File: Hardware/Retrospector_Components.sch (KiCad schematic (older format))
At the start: 147 parts, among them J1 Conn_01x08_Male, J2 Conn_01x08_Male, J3 Conn_01x08_Male, J4 Conn_01x08_Male, J5 SWD_Header, J6 USB_B_Micro, J7 Eurorack_10_pin_power, J8 I2C_TestPoint, U1 MCP6004, U10 LD1117-3.3-4Tab, U2 TL074, U3 MCP6004, U4 IS42S16800F-7TLI, U5 STM32H743ZITx, U6 TL072, U7 AS3364, U8 PCM5100APW, U9 LM2675M-5, Y1 8MHz 20pF

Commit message: Updates to control and panel PCBs
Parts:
- C43: footprint Capacitors_SMD:CP_Elec_5x5.7 -> Capacitors_SMD:CP_Elec_5x5.8; Part_Number C178597 -> (none)
- C61: footprint Capacitors_SMD:CP_Elec_4x5.8 -> Capacitors_SMD:CP_Elec_5x5.8; Part_Number C178597 -> (none)
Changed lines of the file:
@@
 F 0 "C61" H 4250 11700 50  0000 C CNN
 F 1 "47uF" H 4250 11600 50  0000 C CNN
-F 2 "Capacitors_SMD:CP_Elec_4x5.8" H 4438 11550 50  0001 C CNN
-F 3 "https://datasheet.lcsc.com/szlcsc/1809131544_PANASONIC-EEEFT1V220AR_C178597.pdf" H 4400 11700 50  0001 C CNN
-F 4 "C178597" H 4400 11700 50  0001 C CNN "Part_Number"
+F 2 "Capacitors_SMD:CP_Elec_5x5.8" H 4438 11550 50  0001 C CNN
+F 3 "" H 4400 11700 50  0001 C CNN
+F 4 "" H 4400 11700 50  0001 C CNN "Part_Number"
 F 5 "90" H 4400 11700 50  0001 C CNN "Rotation"
 	1    4400 11700
@@
 F 0 "C43" V 1695 9900 50  0000 C CNN
 F 1 "47uF" V 1786 9900 50  0000 C CNN
-F 2 "Capacitors_SMD:CP_Elec_5x5.7" H 1988 9750 50  0001 C CNN
-F 3 "https://datasheet.lcsc.com/szlcsc/1809131544_PANASONIC-EEEFT1V220AR_C178597.pdf" H 1950 9900 50  0001 C CNN
-F 4 "C178597" H 1950 9900 50  0001 C CNN "Part_Number"
+F 2 "Capacitors_SMD:CP_Elec_5x5.8" H 1988 9750 50  0001 C CNN
+F 3 "" H 1950 9900 50  0001 C CNN
+F 4 "" H 1950 9900 50  0001 C CNN "Part_Number"
 F 5 "360" H 1950 9900 50  0001 C CNN "Rotation"
 	1    1950 9900

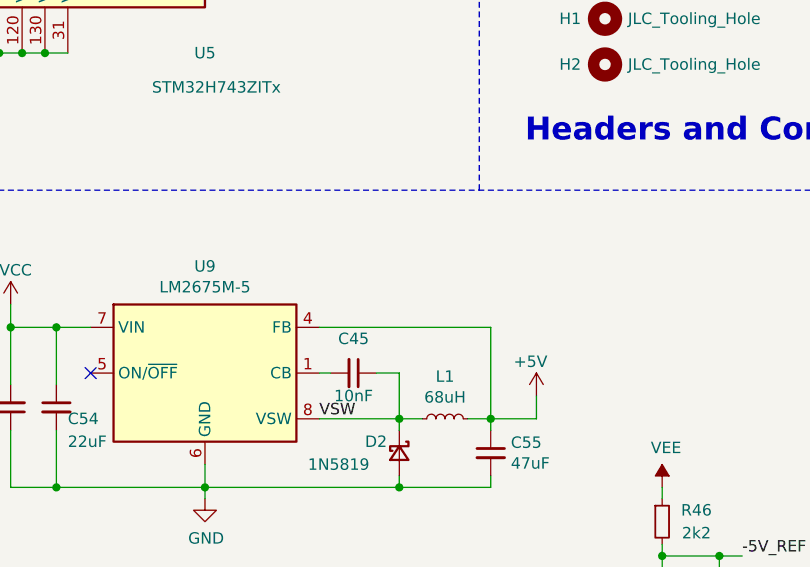
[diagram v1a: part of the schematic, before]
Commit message: Final updates to v2 PCBs for production; USB DFU Mode working
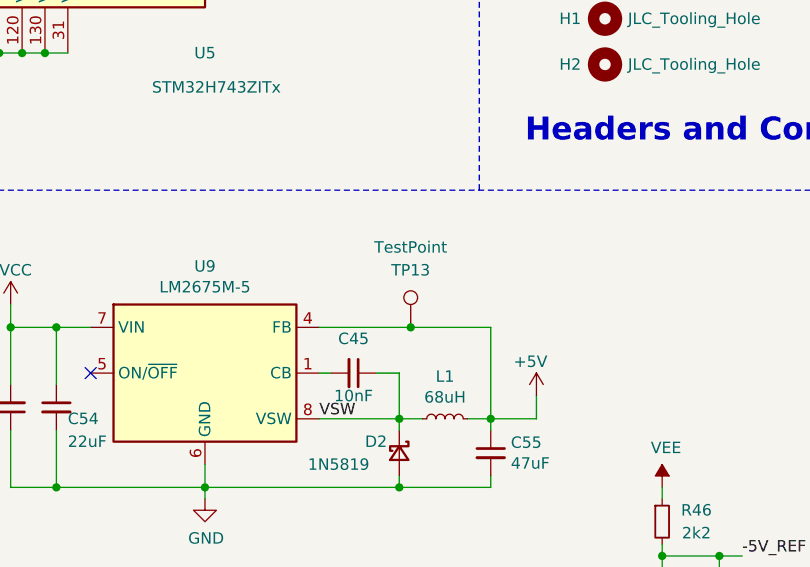
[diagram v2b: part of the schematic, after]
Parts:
- added TP13: TestPoint, Measurement_Points:Measurement_Point_Square-SMD-Pad_Small, symbol Connector:TestPoint
- C43: Part_Number (none) -> C134798
- C57: Part_Number C178597 -> C134793; Rotation 360 -> 270
- C61: Part_Number (none) -> C134798; Rotation 90 -> 360
- C62: Part_Number C178597 -> C134793; Rotation 90 -> 180
- D4: Part_Number C69316 -> C156291
- L1: Part_Number C326343 -> (none)
- R45: Part_Number (none) -> C22775
- U1, U3: Part_Number C7378 -> C116668
- U4: Part_Number C69411 -> C91278
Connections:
- wire segments 652 -> 653
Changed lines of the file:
@@
 F 2 "SMD_Packages:SOIC-14_N" H 9950 5400 50  0001 C CNN
 F 3 "http://ww1.microchip.com/downloads/en/DeviceDoc/21733j.pdf" H 10050 5500 50  0001 C CNN
-F 4 "C7378" H 10000 5300 50  0001 C CNN "Part_Number"
+F 4 "C116668" H 10000 5300 50  0001 C CNN "Part_Number"
 	3    10000 5300
 	1    0    0    1
@@
 F 2 "TO_SOT_Packages_SMD:SOT-23" H 6050 11050 50  0001 C CIN
 F 3 "http://www.ti.com/lit/ds/symlink/lm4040-n.pdf" H 6050 11250 50  0001 C CIN
-F 4 "C69316" H 6050 11250 50  0001 C CNN "Part_Number"
+F 4 "C156291" H 6050 11250 50  0001 C CNN "Part_Number"
 F 5 "90" H 6050 11250 50  0001 C CNN "Rotation"
 	1    6050 11250
@@
 F 2 "SMD_Packages:SOIC-14_N" H 12400 3750 50  0001 C CNN
 F 3 "http://ww1.microchip.com/downloads/en/DeviceDoc/21733j.pdf" H 12500 3850 50  0001 C CNN
-F 4 "C7378" H 12450 3650 50  0001 C CNN "Part_Number"
+F 4 "C116668" H 12450 3650 50  0001 C CNN "Part_Number"
 	4    12450 3650
 	1    0    0    1
@@
 F 2 "Capacitors_SMD:CP_Elec_5x5.8" H 4438 11550 50  0001 C CNN
 F 3 "" H 4400 11700 50  0001 C CNN
-F 4 "" H 4400 11700 50  0001 C CNN "Part_Number"
-F 5 "90" H 4400 11700 50  0001 C CNN "Rotation"
+F 4 "C134798" H 4400 11700 50  0001 C CNN "Part_Number"
+F 5 "360" H 4400 11700 50  0001 C CNN "Rotation"
 	1    4400 11700
 	1    0    0    -1
@@
 F 2 "SMD_Packages:SOIC-14_N" H 9900 2050 50  0001 C CNN
 F 3 "http://ww1.microchip.com/downloads/en/DeviceDoc/21733j.pdf" H 10000 2150 50  0001 C CNN
-F 4 "C7378" H 9950 1950 50  0001 C CNN "Part_Number"
+F 4 "C116668" H 9950 1950 50  0001 C CNN "Part_Number"
 F 5 "" H 9950 1950 50  0001 C CNN "Rotation"
 	2    9950 1950
@@
 F 2 "SMD_Packages:SOIC-14_N" H 9950 3700 50  0001 C CNN
 F 3 "http://ww1.microchip.com/downloads/en/DeviceDoc/21733j.pdf" H 10050 3800 50  0001 C CNN
-F 4 "C7378" H 10000 3600 50  0001 C CNN "Part_Number"
+F 4 "C116668" H 10000 3600 50  0001 C CNN "Part_Number"
 	1    10000 3600
 	1    0    0    1
@@
 F 2 "SMD_Packages:SOIC-14_N" H 7250 10350 50  0001 C CNN
 F 3 "http://ww1.microchip.com/downloads/en/DeviceDoc/21733j.pdf" H 7350 10450 50  0001 C CNN
-F 4 "C7378" H 7300 10250 50  0001 C CNN "Part_Number"
+F 4 "C116668" H 7300 10250 50  0001 C CNN "Part_Number"
 	5    7300 10250
 	1    0    0    -1
@@
 F 2 "Capacitors_SMD:CP_Elec_5x5.8" H 1988 9750 50  0001 C CNN
 F 3 "" H 1950 9900 50  0001 C CNN
-F 4 "" H 1950 9900 50  0001 C CNN "Part_Number"
+F 4 "C134798" H 1950 9900 50  0001 C CNN "Part_Number"
 F 5 "360" H 1950 9900 50  0001 C CNN "Rotation"
 	1    1950 9900
@@
 F 2 "Capacitors_SMD:CP_Elec_4x5.8" H 1988 11050 50  0001 C CNN
 F 3 "https://datasheet.lcsc.com/szlcsc/1809131544_PANASONIC-EEEFT1V220AR_C178597.pdf" H 1950 11200 50  0001 C CNN
-F 4 "C178597" H 1950 11200 50  0001 C CNN "Part_Number"
-F 5 "360" H 1950 11200 50  0001 C CNN "Rotation"
+F 4 "C134793" H 1950 11200 50  0001 C CNN "Part_Number"
+F 5 "270" H 1950 11200 50  0001 C CNN "Rotation"
 	1    1950 11200
 	0    -1   -1   0
@@
 F 2 "Capacitors_SMD:CP_Elec_4x5.8" H 4938 11550 50  0001 C CNN
 F 3 "https://datasheet.lcsc.com/szlcsc/1809131544_PANASONIC-EEEFT1V220AR_C178597.pdf" H 4900 11700 50  0001 C CNN
-F 4 "C178597" H 4900 11700 50  0001 C CNN "Part_Number"
-F 5 "90" H 4900 11700 50  0001 C CNN "Rotation"
+F 4 "C134793" H 4900 11700 50  0001 C CNN "Part_Number"
+F 5 "180" H 4900 11700 50  0001 C CNN "Rotation"
 	1    4900 11700
 	1    0    0    -1
@@
 F 2 "Custom_Footprints:TSOP-II-54_22.2x10.16mm_P0.8mm" H 6950 3150 50  0001 C CNN
 F 3 "https://lcsc.com/product-detail/DDR_ISSI-Integrated-Silicon-Solution-IS42S16800F-7TLI_C69411.html" H 6350 4400 50  0001 C CNN
-F 4 "C69411" H 6950 3150 50  0001 C CNN "Part_Number"
+F 4 "C91278" H 6950 3150 50  0001 C CNN "Part_Number"
 	1    6950 3150
 	1    0    0    -1
@@
 F 2 "SMD_Packages:SOIC-14_N" H 12400 1950 50  0001 C CNN
 F 3 "http://ww1.microchip.com/downloads/en/DeviceDoc/21733j.pdf" H 12500 2050 50  0001 C CNN
-F 4 "C7378" H 12450 1850 50  0001 C CNN "Part_Number"
+F 4 "C116668" H 12450 1850 50  0001 C CNN "Part_Number"
 	2    12450 1850
 	1    0    0    1
@@
 F 2 "SMD_Packages:SOIC-14_N" H 8150 10350 50  0001 C CNN
 F 3 "http://ww1.microchip.com/downloads/en/DeviceDoc/21733j.pdf" H 8250 10450 50  0001 C CNN
-F 4 "C7378" H 8200 10250 50  0001 C CNN "Part_Number"
+F 4 "C116668" H 8200 10250 50  0001 C CNN "Part_Number"
 	5    8200 10250
 	1    0    0    -1
@@
 F 2 "SMD_Packages:SOIC-14_N" H 9950 7050 50  0001 C CNN
 F 3 "http://ww1.microchip.com/downloads/en/DeviceDoc/21733j.pdf" H 10050 7150 50  0001 C CNN
-F 4 "C7378" H 10000 6950 50  0001 C CNN "Part_Number"
+F 4 "C116668" H 10000 6950 50  0001 C CNN "Part_Number"
 	4    10000 6950
 	1    0    0    1
@@
 F 2 "SMD_Packages:SOIC-14_N" H 12450 7050 50  0001 C CNN
 F 3 "http://ww1.microchip.com/downloads/en/DeviceDoc/21733j.pdf" H 12550 7150 50  0001 C CNN
-F 4 "C7378" H 12500 6950 50  0001 C CNN "Part_Number"
+F 4 "C116668" H 12500 6950 50  0001 C CNN "Part_Number"
 	3    12500 6950
 	1    0    0    1
@@
 F 2 "SMD_Packages:SOIC-14_N" H 12450 5400 50  0001 C CNN
 F 3 "http://ww1.microchip.com/downloads/en/DeviceDoc/21733j.pdf" H 12550 5500 50  0001 C CNN
-F 4 "C7378" H 12500 5300 50  0001 C CNN "Part_Number"
+F 4 "C116668" H 12500 5300 50  0001 C CNN "Part_Number"
 	1    12500 5300
 	1    0    0    -1
@@
 F 2 "Resistors_SMD:R_0603_HandSoldering" H 10700 10350 50  0001 C CNN
 F 3 "~" H 10700 10350 50  0001 C CNN
-F 4 "" H 10700 10350 50  0001 C CNN "Part_Number"
+F 4 "C22775" H 10700 10350 50  0001 C CNN "Part_Number"
 	1    10700 10350
 	-1   0    0    1
@@
 	5300 10450 5300 10050
 Wire Wire Line
-	5300 10050 4550 10050
+	5300 10050 4950 10050
 Connection ~ 5300 10450
 Wire Wire Line
@@
 F 2 "Custom_Footprints:TDK_Inductor_6.9x7.2" H 5100 10450 50  0001 C CNN
 F 3 "https://www.mouser.co.uk/ProductDetail/810-CLF7045T-680M-D/" H 5100 10450 50  0001 C CNN
-F 4 "C326343" V 5100 10450 50  0001 C CNN "Part_Number"
+F 4 "" V 5100 10450 50  0001 C CNN "Part_Number"
 	1    5100 10450
 	0    -1   -1   0
@@
 	-1   0    0    -1
 $EndComp
+$Comp
+L Connector:TestPoint TP13
+U 1 1 6062BFFE
+P 4950 10050
+F 0 "TP13" H 4950 10300 50  0000 C CNN
+F 1 "TestPoint" H 4950 10400 50  0000 C CNN
+F 2 "Measurement_Points:Measurement_Point_Square-SMD-Pad_Small" H 5150 10050 50  0001 C CNN
+F 3 "~" H 5150 10050 50  0001 C CNN
+	1    4950 10050
+	1    0    0    -1
+$EndComp
+Connection ~ 4950 10050
+Wire Wire Line
+	4950 10050 4550 10050
 $EndSCHEMATC

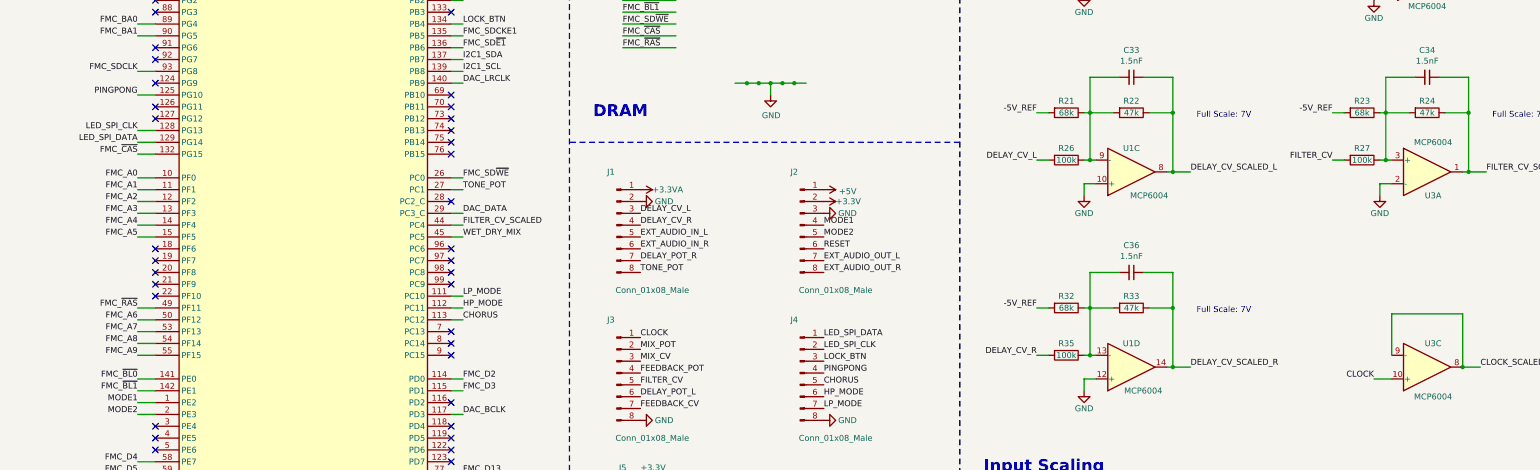
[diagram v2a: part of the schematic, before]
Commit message: Updated IO assignments; corrected position of 'Stereo wide' and 'Chorus' switches
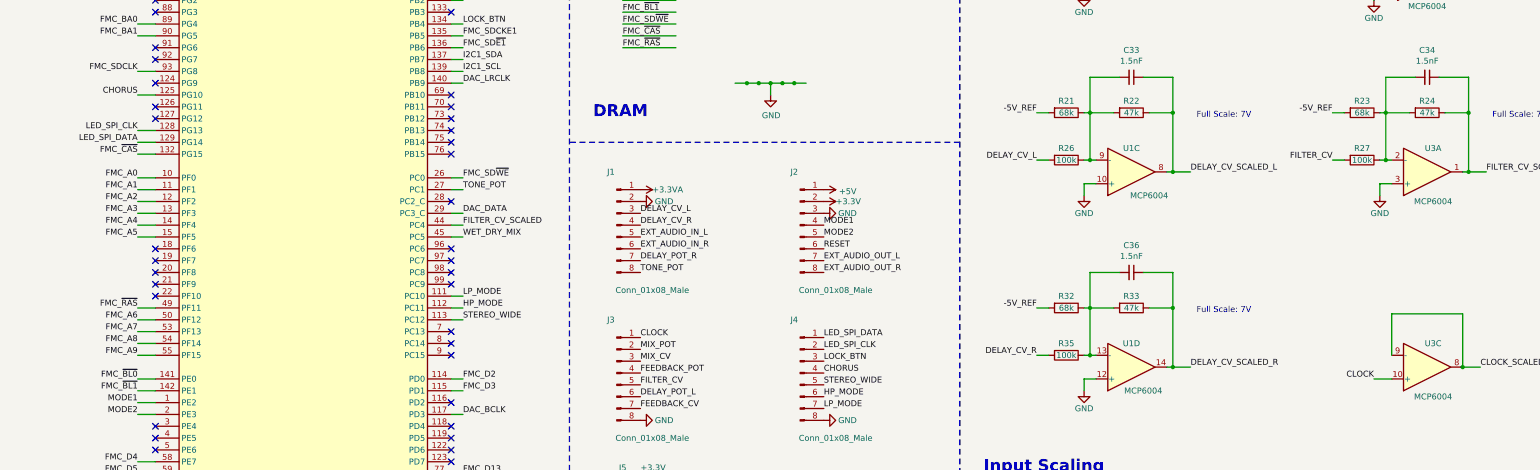
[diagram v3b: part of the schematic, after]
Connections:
- net labels added: STEREO_WIDE
- net labels removed: PINGPONG
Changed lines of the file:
@@
 encoding utf-8
 Sheet 1 1
-Title "Retrospector"
+Title "Retrospector v3"
 Date ""
-Rev "2"
+Rev "3"
 Comp "Mountjoy Modular"
 Comment1 ""
@@
 	14900 1750 14950 1750
 Text Label 7400 7100 0    50   ~ 0
-CHORUS
+STEREO_WIDE
 $Comp
 L Connector:Conn_01x08_Male J1
@@
 F 4 "C116668" H 12500 5300 50  0001 C CNN "Part_Number"
 	1    12500 5300
-	1    0    0    -1
+	1    0    0    1
 $EndComp
 Connection ~ 1200 1000
@@
 	4350 2150 4250 2150
 Text Label 4350 6550 0    50   ~ 0
-CHORUS
+STEREO_WIDE
 Wire Wire Line
 	4250 6550 4350 6550
@@
 FLT: connect to earth for \nhigher latency but less ringing
 Text Label 7400 7000 0    50   ~ 0
-PINGPONG
+CHORUS
 Text Label 7400 7300 0    50   ~ 0
 LP_MODE
@@
 FILTER_CV_SCALED
 Text Label 1600 4650 2    50   ~ 0
-PINGPONG
+CHORUS
 $Comp
 L power:GND #PWR050

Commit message: Updated SDRAM to work with 32MB RAM (implemented A12 line); attempts to get SPI DMA working for LED controller
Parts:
- U4: symbol Memory_RAM:IS42S16400J-xC -> SDRAM:IS42S16160
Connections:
- net labels added: FMC_A12
- wire segments 653 -> 655
- no-connect marks 44 -> 43
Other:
- note added: "FLT: connect to ground for \nhigher latency but less ringing"
- note removed: "FLT: connect to earth for \nhigher latency but less ringing"
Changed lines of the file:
@@
 Connection ~ 1700 10700
 $Comp
-L Memory_RAM:IS42S16400J-xC U4
+L SDRAM:IS42S16160 U4
 U 1 1 5F0FFF4D
 P 6950 3150
@@
 Wire Wire Line
 	4350 3750 4250 3750
-NoConn ~ 1750 3850
 NoConn ~ 1750 3950
 NoConn ~ 1750 4250
@@
 $EndComp
 Text Notes 13600 10900 0    50   ~ 0
-FLT: connect to earth for \nhigher latency but less ringing
+FLT: connect to ground for \nhigher latency but less ringing
 Text Label 7400 7000 0    50   ~ 0
 CHORUS
@@
 Wire Wire Line
 	4950 10050 4550 10050
+Text Label 5800 3450 0    50   ~ 0
+FMC_A12
+Wire Wire Line
+	6150 3450 5800 3450
+Text Label 1600 3850 2    50   ~ 0
+FMC_A12
+Wire Wire Line
+	1750 3850 1600 3850
 $EndSCHEMATC
